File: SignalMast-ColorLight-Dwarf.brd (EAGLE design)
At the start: 12.7 x 25.7 mm, 4 parts

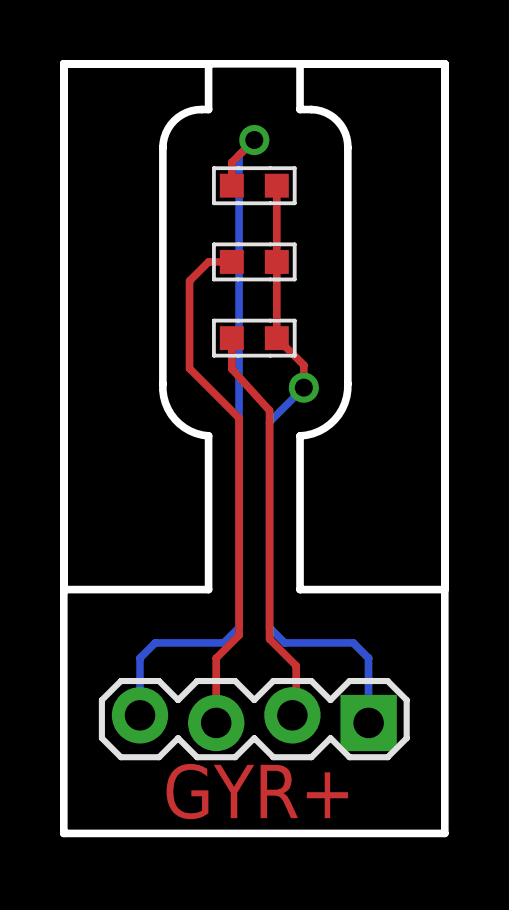
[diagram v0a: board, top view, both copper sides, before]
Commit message: normalized values
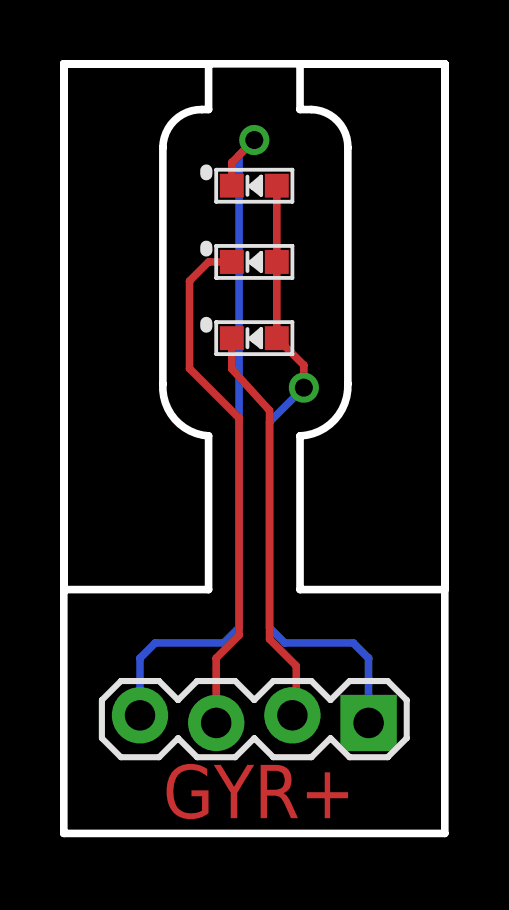
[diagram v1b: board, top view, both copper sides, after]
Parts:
- GYR+: value CONNECTOR-GROVE-4P-2.0-3470130P1 -> 0.100
- turned LED1 to 0 degrees
- turned LED2 to 0 degrees
- turned LED3 to 0 degrees
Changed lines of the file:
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@@
 </autorouter>
 <elements>
-<element name="GYR+" library="SPCoast" package="1X04_LOCK" value="CONNECTOR-GROVE-4P-2.0-3470130P1" x="10.16" y="3.81" smashed="yes" rot="R180"/>
-<element name="LED1" library="SPCoast" package="0603-LED" value="R" x="6.35" y="16.51" smashed="yes" rot="R180">
-<attribute name="OPL" value="19-217-R6C-AL1M2VY-3T" x="6.35" y="16.51" size="1.778" layer="27" rot="R180" display="off"/>
-<attribute name="VALUE" x="11.43" y="17.145" size="1.27" layer="27" rot="R180"/>
+<element name="GYR+" library="SPCoast" package="1X04_LOCK" value="0.100" x="10.16" y="3.81" smashed="yes" rot="R180"/>
+<element name="LED1" library="SPCoast" package="0603-LED" value="R" x="6.35" y="16.51" smashed="yes">
+<attribute name="OPL" value="19-217-R6C-AL1M2VY-3T" x="6.35" y="16.51" size="1.778" layer="27" display="off"/>
+<attribute name="VALUE" x="1.27" y="15.875" size="1.27" layer="27"/>
 </element>
-<element name="LED2" library="SPCoast" package="0603-LED" value="Y" x="6.35" y="19.05" smashed="yes" rot="R180">
-<attribute name="OPL" value="19-217-Y5C-AM1N1VY-3T" x="6.35" y="19.05" size="1.778" layer="27" rot="R180" display="off"/>
-<attribute name="VALUE" x="11.43" y="19.685" size="1.27" layer="27" rot="R180"/>
+<element name="LED2" library="SPCoast" package="0603-LED" value="Y" x="6.35" y="19.05" smashed="yes">
+<attribute name="OPL" value="19-217-Y5C-AM1N1VY-3T" x="6.35" y="19.05" size="1.778" layer="27" display="off"/>
+<attribute name="VALUE" x="1.27" y="18.415" size="1.27" layer="27"/>
 </element>
-<element name="LED3" library="SPCoast" package="0603-LED" value="G" x="6.35" y="21.59" smashed="yes" rot="R180">
-<attribute name="OPL" value="19-217-G7C-AN1P2-3T " x="6.35" y="21.59" size="1.778" layer="27" rot="R180" display="off"/>
-<attribute name="VALUE" x="11.43" y="22.225" size="1.27" layer="27" rot="R180"/>
+<element name="LED3" library="SPCoast" package="0603-LED" value="G" x="6.35" y="21.59" smashed="yes">
+<attribute name="OPL" value="19-217-G7C-AN1P2-3T " x="6.35" y="21.59" size="1.778" layer="27" display="off"/>
+<attribute name="VALUE" x="1.27" y="20.955" size="1.27" layer="27"/>
 </element>
 </elements>
